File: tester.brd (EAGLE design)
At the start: 56 x 67 mm, 71 parts, among them IC1 ATmega8/88/168, K1 NA 05W K, M1 SP6000C-180, P1 250, P2 10k lin, Q1 BC847CSMD, Q2 BC847CSMD, Q3 BC807-40SMD, Q4 8,000 MHz, Q5 BC847CSMD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

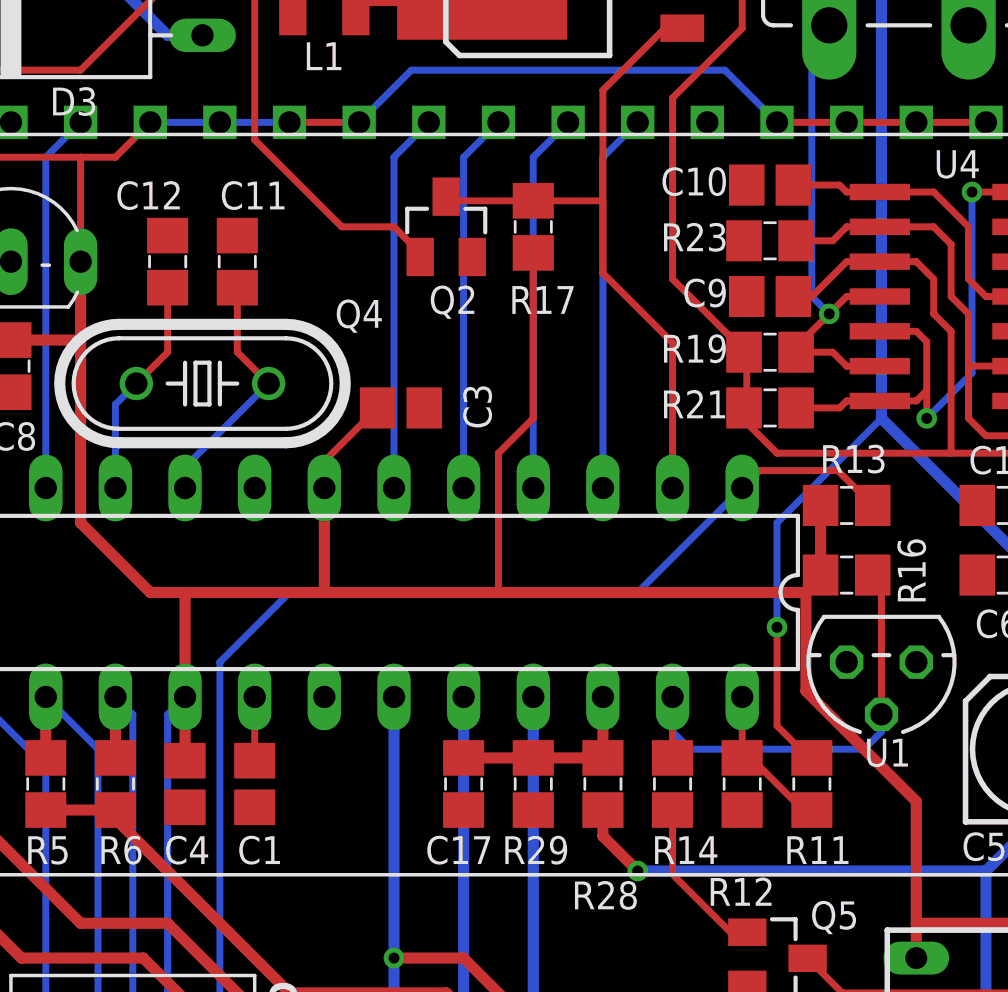
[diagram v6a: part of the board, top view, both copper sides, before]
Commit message: no more c from resistor lib, all rcl now
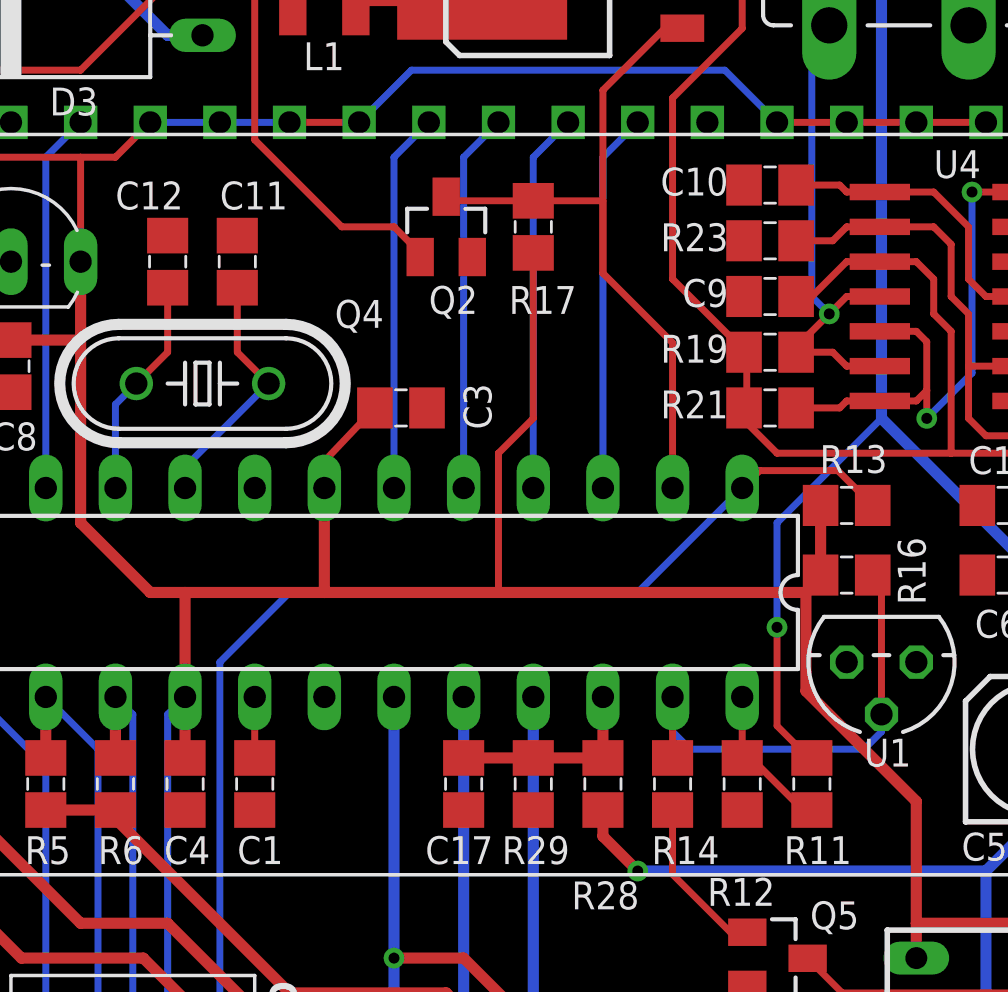
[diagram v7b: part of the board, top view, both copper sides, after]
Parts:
- C1, C10, C3, C4, C9: device resistor:C0805 -> rcl:C0805
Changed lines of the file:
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@@
 </autorouter>
 <elements>
-<element name="C3" library="resistor" package="C0805" value="100n" x="25.654" y="39.116" smashed="yes" rot="R180">
+<element name="C3" library="rcl" package="C0805" value="100n" x="25.654" y="39.116" smashed="yes" rot="R180">
 <attribute name="NAME" x="27.94" y="40.005" size="1.016" layer="25" rot="R270"/>
 <attribute name="VALUE" x="26.543" y="41.148" size="1.27" layer="27" rot="R180"/>
@@
 <attribute name="VALUE" x="41.021" y="33.528" size="1.27" layer="27"/>
 </element>
-<element name="C1" library="resistor" package="C0805" value="1n" x="20.32" y="25.4" smashed="yes" rot="R90">
+<element name="C1" library="rcl" package="C0805" value="1n" x="20.32" y="25.4" smashed="yes" rot="R90">
 <attribute name="NAME" x="19.685" y="22.479" size="1.016" layer="25"/>
 <attribute name="VALUE" x="22.352" y="24.511" size="1.27" layer="27" rot="R90"/>
@@
 <attribute name="VALUE" x="28.448" y="46.609" size="1.27" layer="27" rot="R270"/>
 </element>
-<element name="C4" library="resistor" package="C0805" value="100n" x="17.78" y="25.4" smashed="yes" rot="R270">
+<element name="C4" library="rcl" package="C0805" value="100n" x="17.78" y="25.4" smashed="yes" rot="R270">
 <attribute name="NAME" x="17.018" y="22.479" size="1.016" layer="25"/>
 <attribute name="VALUE" x="15.748" y="26.289" size="1.27" layer="27" rot="R270"/>
@@
 <variant name="nopwm" populate="no"/>
 </element>
-<element name="C9" library="resistor" package="C0805" value="100n" x="39.116" y="43.18" smashed="yes" rot="R180">
+<element name="C9" library="rcl" package="C0805" value="100n" x="39.116" y="43.18" smashed="yes" rot="R180">
 <attribute name="NAME" x="37.592" y="43.815" size="1.016" layer="25" rot="R180"/>
 <attribute name="VALUE" x="40.005" y="45.212" size="1.27" layer="27" rot="R180"/>
@@
 <variant name="nopwm" populate="no"/>
 </element>
-<element name="C10" library="resistor" package="C0805" value="100n" x="39.116" y="47.244" smashed="yes" rot="R180">
+<element name="C10" library="rcl" package="C0805" value="100n" x="39.116" y="47.244" smashed="yes" rot="R180">
 <attribute name="NAME" x="37.592" y="47.879" size="1.016" layer="25" rot="R180"/>
 <attribute name="VALUE" x="40.005" y="49.276" size="1.27" layer="27" rot="R180"/>
@@
 <wire x1="17.145" y1="13.335" x2="17.145" y2="27.94" width="0.254" layer="16"/>
 <wire x1="17.145" y1="27.94" x2="17.78" y2="28.575" width="0.254" layer="16"/>
-<wire x1="17.78" y1="28.575" x2="17.78" y2="26.25" width="0.4064" layer="1"/>
+<wire x1="17.78" y1="28.575" x2="17.78" y2="26.35" width="0.4064" layer="1"/>
 <wire x1="13.97" y1="48.26" x2="15.24" y2="48.26" width="0.254" layer="1"/>
 <wire x1="15.24" y1="48.26" x2="16.51" y2="49.53" width="0.254" layer="1"/>
@@
 <wire x1="29.21" y1="37.465" x2="29.21" y2="32.385" width="0.254" layer="1"/>
 <wire x1="22.86" y1="36.195" x2="22.86" y2="37.172" width="0.254" layer="1"/>
-<wire x1="22.86" y1="37.172" x2="24.804" y2="39.116" width="0.254" layer="1"/>
+<wire x1="22.86" y1="37.172" x2="24.704" y2="39.116" width="0.254" layer="1"/>
 <wire x1="29.21" y1="32.385" x2="40.425" y2="32.385" width="0.4064" layer="1"/>
 <wire x1="13.97" y1="34.925" x2="13.97" y2="41.59" width="0.4064" layer="1"/>
@@
 <signal name="AREF">
 <contactref element="C1" pad="2"/>
-<wire x1="20.32" y1="28.575" x2="20.32" y2="26.25" width="0.254" layer="1"/>
+<wire x1="20.32" y1="28.575" x2="20.32" y2="26.35" width="0.254" layer="1"/>
 <contactref element="IC1" pad="21"/>
 </signal>
@@
 <wire x1="43.12" y1="46.99" x2="41.91" y2="46.99" width="0.254" layer="1"/>
 <wire x1="41.91" y1="46.99" x2="41.656" y2="47.244" width="0.254" layer="1"/>
-<wire x1="41.656" y1="47.244" x2="39.966" y2="47.244" width="0.254" layer="1"/>
+<wire x1="41.656" y1="47.244" x2="40.066" y2="47.244" width="0.254" layer="1"/>
 <wire x1="48.32" y1="39.37" x2="49.696" y2="39.37" width="0.254" layer="1"/>
 <wire x1="48.32" y1="43.18" x2="49.53" y2="43.18" width="0.254" layer="1"/>
@@
 <wire x1="43.12" y1="44.45" x2="41.91" y2="44.45" width="0.254" layer="1"/>
 <wire x1="41.91" y1="44.45" x2="40.64" y2="43.18" width="0.254" layer="1"/>
-<wire x1="40.64" y1="43.18" x2="39.966" y2="43.18" width="0.254" layer="1"/>
+<wire x1="40.64" y1="43.18" x2="40.066" y2="43.18" width="0.254" layer="1"/>
 <wire x1="53.274" y1="43.18" x2="53.274" y2="41.148" width="0.254" layer="1"/>
 <wire x1="53.274" y1="41.148" x2="53.274" y2="39.116" width="0.254" layer="1"/>
